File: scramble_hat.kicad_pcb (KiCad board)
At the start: 4 copper layers, 51.4 x 21.1 mm, 53 parts, among them J1 NCJ6FA-H, J2 TRRS PJ-3X4S (CTIA, bottom-si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, J3 Carrier LEFT 1-7, J4 Carrier RIGHT 1-7, J5 VDD_PoE / PGND, Q1 DMP3098 (P-FET 60V), SW1 SS-12D00-G3, U1 ES8389, U2 TPS7A2033

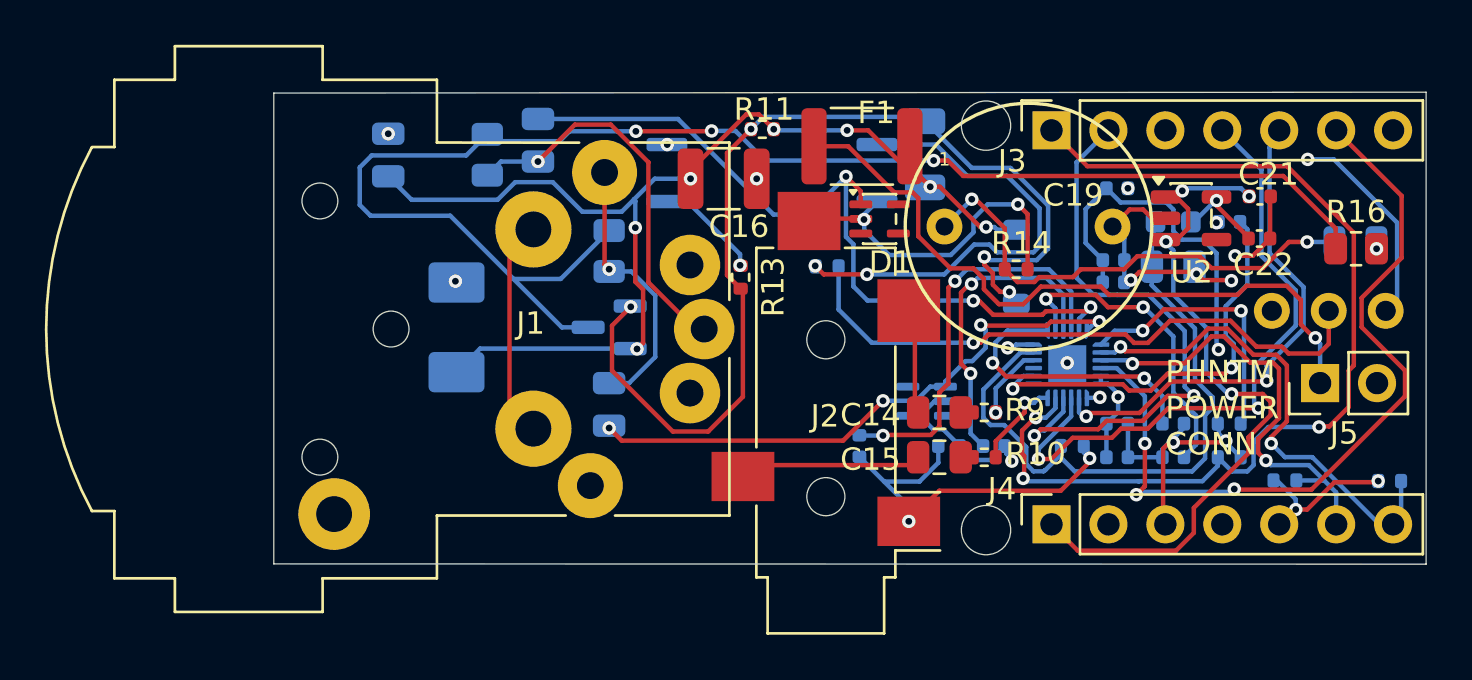
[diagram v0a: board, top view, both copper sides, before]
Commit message: fix: phantom drive — correct D7/OK1 orientation, 80V opto, drop C16
- D7 zener was reversed (Vgs clamped at -0.7V, FET never switched);
  cathode now to V_FILT, anode to Q1_GATE.
- OK1 optocoupler C/E were swapped in the symbol (pin3/pin4), exceeding
  its 6V emitter-collector reverse rating on the PoE rail and holding
  phantom on in both switch positions; collector->R13/gate, emitter->PGND.
- OK1 -> TLP291 (80V Vceo), SOP-4 1.27mm; LTV-817's 35V was under-rated
  for the 46-57V PoE rail.
- Remove C16 (10uF): it sat on the tapped bus and broke 802.3 PoE
  detection (>0.15uF), which blocked cold-start with the tap connected.
- Regenerate fab set (gerbers, drills, CPL, BOM) for the above.
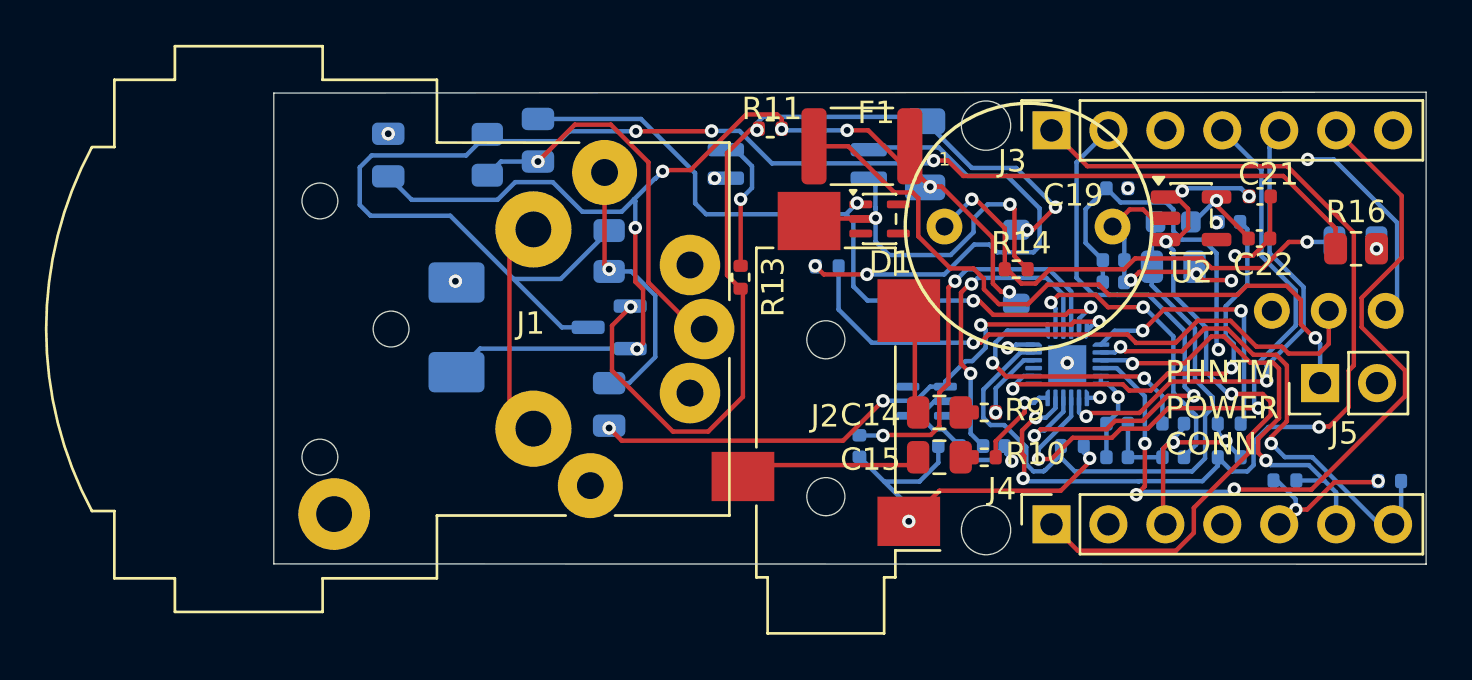
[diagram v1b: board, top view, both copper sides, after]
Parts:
- removed C16: 10uF/100V, Capacitor_SMD:C_1210_3225Metric
- OK1: value LTV-817S -> TLP291; footprint Package_SO:SO-4_7.6x3.6mm_P2.54mm -> Package_SO:SOP-4_4.4x2.6mm_P1.27mm
- moved OK1 1.20 mm to (104.2, 83.4)
- moved R11 0.35 mm to (103.0, 81.8)
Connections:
- D7 pad 1: Q1_GATE -> V_FILT
- D7 pad 2: V_FILT -> Q1_GATE
- OK1 pad 3: OK1_COLLECTOR -> PGND
- OK1 pad 4: PGND -> OK1_COLLECTOR
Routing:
- net Q1_GATE: track 46.7 -> 40.7 mm
- net V_FILT: track 50.1 -> 52.8 mm
- net MIC1N: track 35.4 -> 33.3 mm
- net OK1_COLLECTOR: track 4.73 -> 6.13 mm
- net AGND: track 62.3 -> 63.3 mm
- net PGND: track 21.9 -> 22.4 mm, vias 6 -> 5

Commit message: codec: add J6 4-pin I2C header (3V3/AGND/SDA/SCL) for external display
- New scramble_hat:Conn_01x04 symbol + J6 in sheet_codec, connected to
  +3V3/AGND/SDA/SCL; placed on F.Cu and routed.
- Pin order (AGND/+3V3/SCL/SDA) set to match the external display's
  wiring harness.
- Fab set intentionally NOT regenerated (more design changes pending).
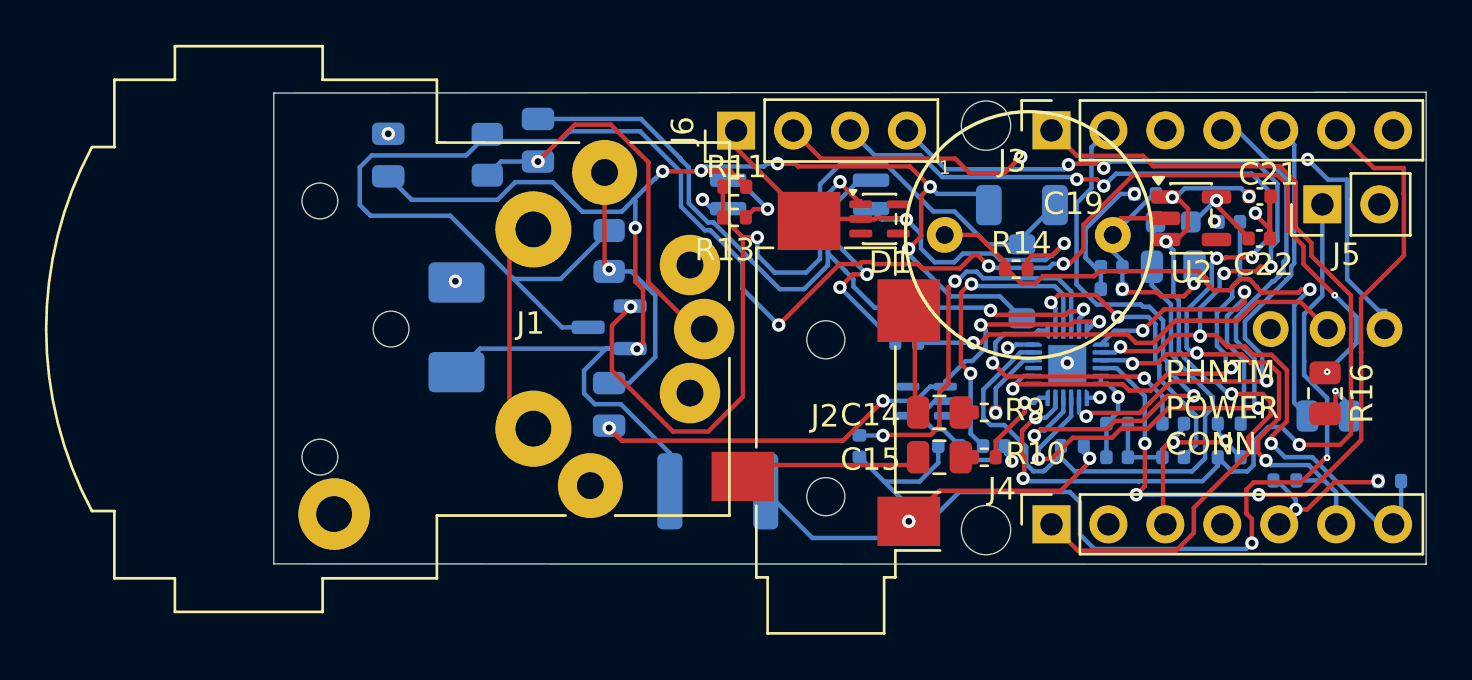
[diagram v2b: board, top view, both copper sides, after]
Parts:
- added J6: I2C 3V3/AGND/SDA/SCL, Connector_PinHeader_2.54mm:PinHeader_1x04_P2.54mm_Vertical, F.Cu at (101.5, 81.9)
- F1: moved to B.Cu
- moved F1 16.7 mm to (100.7, 98.0), turned to 180 degrees
- moved J5 7.98 mm to (127.7, 85.2)
- moved D8 7.86 mm to (127.9, 94.7)
- moved R16 6.60 mm to (127.8, 93.6), turned to -90 degrees
- moved R12 4.92 mm to (109.1, 91.4)
- moved C18 4.88 mm to (114.2, 85.2), turned to 180 degrees
- moved R11 3.04 mm to (101.4, 84.4)
- moved R13 2.69 mm to (101.4, 85.8), turned to 180 degrees
- moved OK1 1.36 mm to (104.3, 84.8)
- moved C1 1.27 mm to (119.8, 84.8)
- moved SW1 0.81 mm to (127.9, 90.8)
- moved D7 0.70 mm to (114.2, 88.7)
- moved C19 0.37 mm to (114.6, 86.6)
- moved C2 0.32 mm to (118.3, 88.0)
- moved C3 0.32 mm to (118.2, 89.0)
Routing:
- net SCL: track 20.2 -> 49.8 mm, vias 2 -> 7
- net SDA: track 22.9 -> 49.9 mm, vias 2 -> 7
- net V_FILT: track 52.8 -> 67.9 mm
- net V_PHANTOM: track 66.6 -> 81.2 mm, vias 3 -> 5
- net V_PoE: track 31.0 -> 44.2 mm, vias 1 -> 2
- net OK1_LED_A: track 21.4 -> 10.6 mm
- net PHANTOM_SW: track 27.4 -> 19.8 mm
- net AGND: track 63.3 -> 70.2 mm, vias 15 -> 13
- net MIC1N: track 33.3 -> 39.4 mm
- net PGND: track 22.4 -> 26.3 mm, vias 5 -> 4
- net OK1_COLLECTOR: track 6.13 -> 3.42 mm
- net PHANTOM_LED: track 0.00 -> 2.58 mm
- net AD0: track 12.1 -> 14.2 mm
- net Q1_GATE: track 40.7 -> 41.9 mm, vias 4 -> 2
- net ASDOUT: track 45.3 -> 46.5 mm
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
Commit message: fab: production prep — white/brighter status LED, C19 assembled, live BOM prices
- D8 red -> white: KT-0805W (C34499, Basic, in stock); old Kingbright
  KP-2012EC (C598272) was out of stock.
- R16 33k -> 15k, 1/4W AC0805 (C20142753) — ~2x brighter phantom-present
  LED (~3mA); resistor dissipates ~193mW at the 57V PoE max.
- C19 -> JEC JY222M2FY5VS7LE (C389727, Y2 300VAC, same 7.5mm land, in
  stock) moved onto JLCPCB THT assembly (off the hand-solder list).
- exclude_from_pos_files on J1/J2/J5 so placement/CPL leaves the
  hand-soldered parts (jacks + PoE header) to hand assembly.
- BOM: added J6, filled all resistor LCSC#s, refreshed unit prices to
  live qty-10 LCSC, corrected the D1/D2 entry.
- Regenerated gerbers/drills/BOM (csv+xlsx) with J6.
- Removed stale kicad-cli CPL — generate placement with the jlcpcb-tools
  plugin (set U1/QFN +270deg) and verify in JLCPCB preview before order.
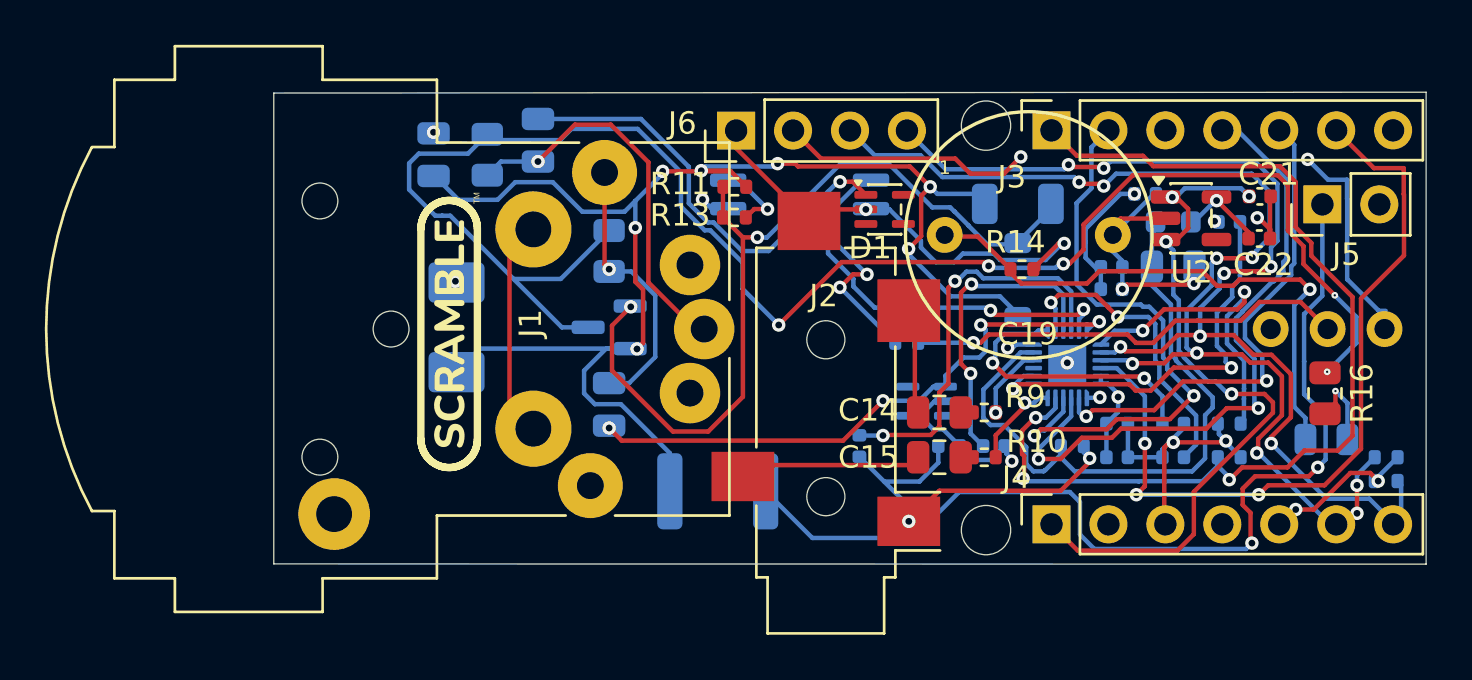
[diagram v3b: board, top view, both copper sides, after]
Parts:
- D8: value LED RED 0805 -> LED white 0805
- R16: value 33k -> 15k
- moved R2 4.63 mm to (130.5, 96.5), turned to 0 degrees
- moved C17 2.02 mm to (88.0, 83.0)
- moved D8 1.05 mm to (127.8, 95.7)
- moved D1 0.48 mm to (108.1, 85.4)
- moved R14 0.25 mm to (114.2, 88.1)
- moved C18 0.19 mm to (114.1, 85.2)
- moved D7 0.19 mm to (114.1, 88.6)
- moved R1 0.16 mm to (130.5, 97.6)
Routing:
- net V_PHANTOM: track 81.2 -> 76.1 mm
- net Q1_GATE: track 41.9 -> 38.2 mm
- net MIC1N: track 39.4 -> 36.2 mm
- net AGND: track 70.2 -> 67.9 mm
- net SCL: track 49.8 -> 51.8 mm, vias 7 -> 9
- net V_FILT: track 67.9 -> 65.9 mm
- net PHANTOM_LED: track 2.58 -> 3.59 mm
- net ASDOUT: track 46.5 -> 46.0 mm
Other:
- board text added: "Hat-trik v2"
- board text added: "ON"
- board text added: "PHTM PWR"
- board text removed: "Hat-trik v1"
- board text removed: "PHNTM POWER"
- board text removed: "PHNTM POWER CONN"

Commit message: fab: remove dangling track stubs; regenerate gerbers
- Cleaned up 2 zero-length dangling track fragments (LRCK, +3V3) left
  from the J6 re-route.
- Regenerated gerbers/drills/zip from the cleaned board.
- DRC: 0 unconnected, no shorts/clearance errors (remaining warnings are
  cosmetic silkscreen + the benign PinSocket library mismatch).
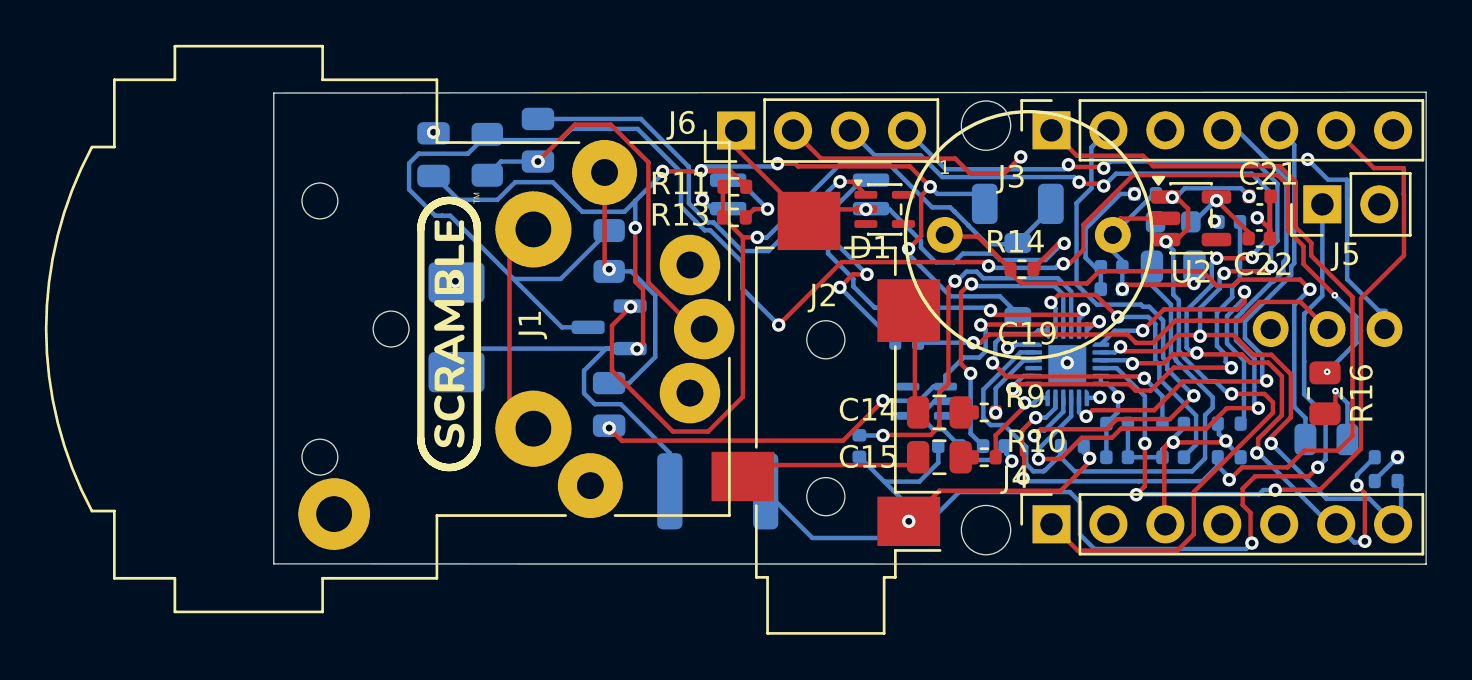
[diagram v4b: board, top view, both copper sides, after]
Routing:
- net +3V3: track 27.3 -> 22.9 mm, vias 5 -> 4
- net SCL: track 51.8 -> 53.6 mm
- net XLR2_HOT: track 12.8 -> 12.2 mm
